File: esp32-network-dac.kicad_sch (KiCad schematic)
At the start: 46 parts, among them J1 USB4510-03-1-A, J2 SJ1-3533NS, J3 Conn_01x04_Male, U1 PCM5122PW, U2 ESP32-WROVER-EM213EH2864PH3Q0, U3 MCP1825S, U4 MCP1825S

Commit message: Changed footrpints to remove DRC warnings. Added board outline.
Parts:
- added H1: MountingHole, symbol Mechanical:MountingHole
- added H2, H3, H4: MountingHole, MountingHole:MountingHole_2.2mm_M2, symbol Mechanical:MountingHole
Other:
- note added: "M2 Mounting Holes"
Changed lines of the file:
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@@
+    (effects (font (size 1.27 1.27) (thickness 0.254) bold) (justify left bottom))
+  )
+  (text "M2 Mounting Holes" (at 133.35 172.72 0)
     (effects (font (size 1.27 1.27) (thickness 0.254) bold) (justify left bottom))
   )
@@
     (pin "1")
   )
+  (symbol (lib_id "Mechanical:MountingHole") (at 135.89 187.96 0) (unit 1)
+    (in_bom yes) (on_board yes) (fields_autoplaced)
+    (property "Reference" "H2" (id 0) (at 138.43 186.6899 0)
+      (effects (font (size 1.27 1.27)) (justify left))
+    )
+    (property "Value" "MountingHole" (id 1) (at 138.43 189.2299 0)
+      (effects (font (size 1.27 1.27)) (justify left))
+    )
+    (property "Footprint" "MountingHole:MountingHole_2.2mm_M2" (id 2) (at 135.89 187.96 0)
+      (effects (font (size 1.27 1.27)) hide)
+    )
+    (property "Datasheet" "~" (id 3) (at 135.89 187.96 0)
+      (effects (font (size 1.27 1.27)) hide)
+    )
+  )
   (symbol (lib_id "power:GND") (at 107.95 134.62 0) (unit 1)
     (in_bom yes) (on_board yes) (fields_autoplaced)
@@
     )
     (pin "1")
+  )
+  (symbol (lib_id "Mechanical:MountingHole") (at 135.89 179.07 0) (unit 1)
+    (in_bom yes) (on_board yes) (fields_autoplaced)
+    (property "Reference" "H1" (id 0) (at 138.43 177.7999 0)
+      (effects (font (size 1.27 1.27)) (justify left))
+    )
+    (property "Value" "MountingHole" (id 1) (at 138.43 180.3399 0)
+      (effects (font (size 1.27 1.27)) (justify left))
+    )
+    (property "Footprint" "" (id 2) (at 135.89 179.07 0)
+      (effects (font (size 1.27 1.27)) hide)
+    )
+    (property "Datasheet" "~" (id 3) (at 135.89 179.07 0)
+      (effects (font (size 1.27 1.27)) hide)
+    )
   )
   (symbol (lib_id "power:+3V3") (at 199.39 20.32 0) (unit 1)
@@
     (pin "2")
   )
+  (symbol (lib_id "Mechanical:MountingHole") (at 154.94 179.07 0) (unit 1)
+    (in_bom yes) (on_board yes) (fields_autoplaced)
+    (property "Reference" "H3" (id 0) (at 157.48 177.7999 0)
+      (effects (font (size 1.27 1.27)) (justify left))
+    )
+    (property "Value" "MountingHole" (id 1) (at 157.48 180.3399 0)
+      (effects (font (size 1.27 1.27)) (justify left))
+    )
+    (property "Footprint" "MountingHole:MountingHole_2.2mm_M2" (id 2) (at 154.94 179.07 0)
+      (effects (font (size 1.27 1.27)) hide)
+    )
+    (property "Datasheet" "~" (id 3) (at 154.94 179.07 0)
+      (effects (font (size 1.27 1.27)) hide)
+    )
+  )
   (symbol (lib_id "power:PWR_FLAG") (at 232.41 144.78 0) (unit 1)
     (in_bom yes) (on_board yes) (fields_autoplaced)
@@
     (pin "3")
     (pin "4")
+  )
+  (symbol (lib_id "Mechanical:MountingHole") (at 154.94 187.96 0) (unit 1)
+    (in_bom yes) (on_board yes) (fields_autoplaced)
+    (property "Reference" "H4" (id 0) (at 157.48 186.6899 0)
+      (effects (font (size 1.27 1.27)) (justify left))
+    )
+    (property "Value" "MountingHole" (id 1) (at 157.48 189.2299 0)
+      (effects (font (size 1.27 1.27)) (justify left))
+    )
+    (property "Footprint" "MountingHole:MountingHole_2.2mm_M2" (id 2) (at 154.94 187.96 0)
+      (effects (font (size 1.27 1.27)) hide)
+    )
+    (property "Datasheet" "~" (id 3) (at 154.94 187.96 0)
+      (effects (font (size 1.27 1.27)) hide)
+    )
   )
   (symbol (lib_id "power:GND") (at 196.85 91.44 0) (unit 1)
@@
       (reference "FB1") (unit 1) (value "120R") (footprint "Resistor_SMD:R_0603_1608Metric")
     )
+    (path "/6d36cd5e-34b5-4051-b036-21bdf59d84b4"
+      (reference "H1") (unit 1) (value "MountingHole") (footprint "MountingHole:MountingHole_2.2mm_M2")
+    )
+    (path "/52e3839b-c2e7-453a-be4e-a57ccb23295f"
+      (reference "H2") (unit 1) (value "MountingHole") (footprint "MountingHole:MountingHole_2.2mm_M2")
+    )
+    (path "/ad63bded-fd94-444e-a2da-8803639d7b67"
+      (reference "H3") (unit 1) (value "MountingHole") (footprint "MountingHole:MountingHole_2.2mm_M2")
+    )
+    (path "/b4c3d837-72a5-4d97-8651-9b49f83ce226"
+      (reference "H4") (unit 1) (value "MountingHole") (footprint "MountingHole:MountingHole_2.2mm_M2")
+    )
     (path "/bccef6fe-1b25-4ae1-a87c-dd8d2ab4d17e"

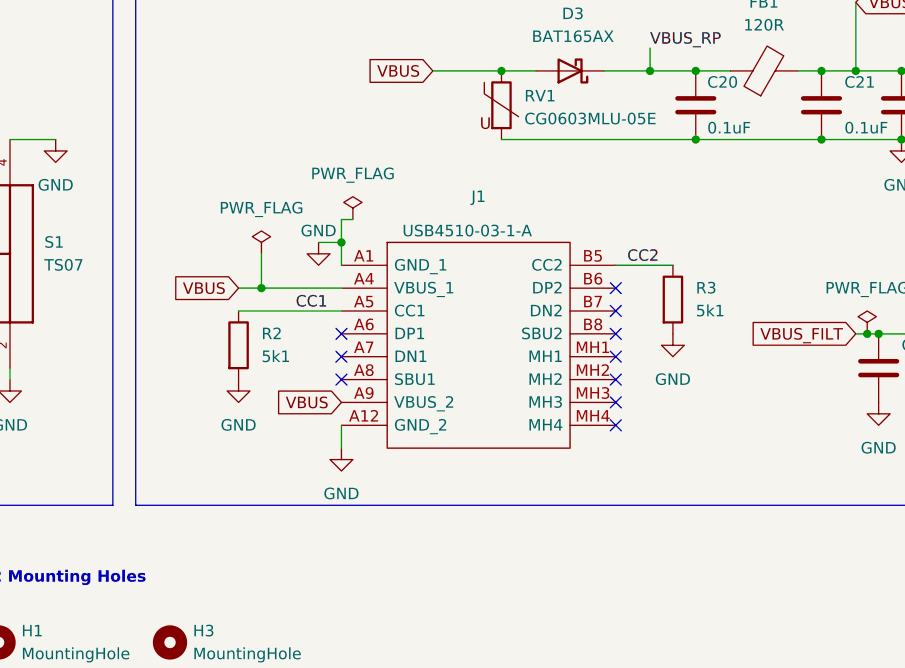
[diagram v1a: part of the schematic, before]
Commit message: Updates to USB C receptive - replaced mid-mount recepticle with SMT
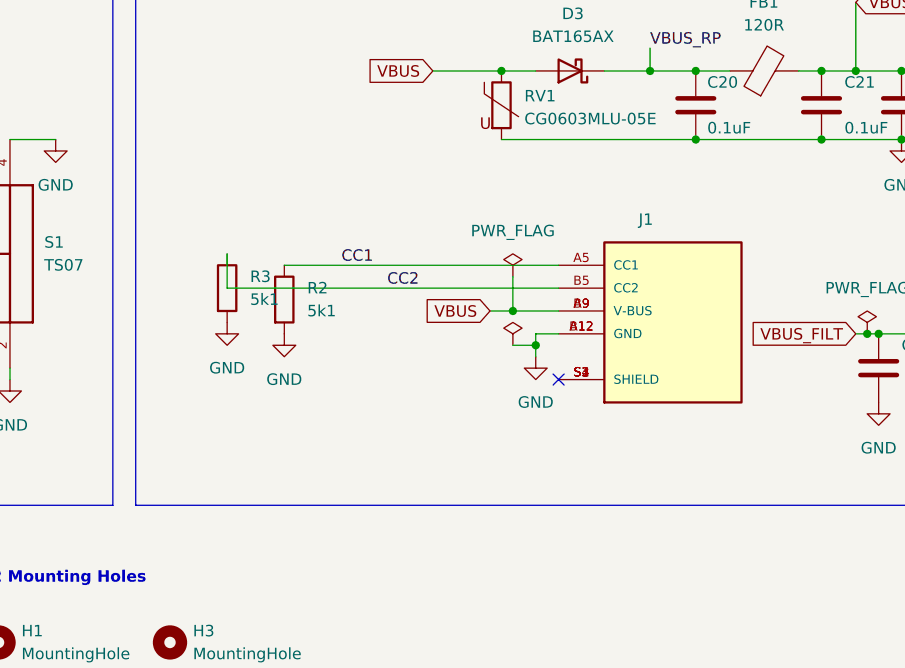
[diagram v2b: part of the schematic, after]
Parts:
- removed J1: USB4510-03-1-A, library:USB4510031A, symbol USB4510-03-1-A:USB4510-03-1-A
- added J1: UJC-HP-3-SMT-TR, library:CUI_UJC-HP-3-SMT-TR, symbol UJC-HP-3-SMT-TR:UJC-HP-3-SMT-TR
- H1: footprint (none) -> MountingHole:MountingHole_2.2mm_M2
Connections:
- net CC1: now also J1.A5 (CC1)
- net CC2: now also J1.B5 (CC2)
- net GND: now also J1.A12 (GND), J1.B12 (GND)
- net VBUS: now also J1.A9 (V-BUS), J1.B9 (V-BUS)
- new net: J1.S1 (SHIELD), J1.S2 (SHIELD), J1.S3 (SHIELD), J1.S4 (SHIELD)
- no-connect marks 28 -> 19

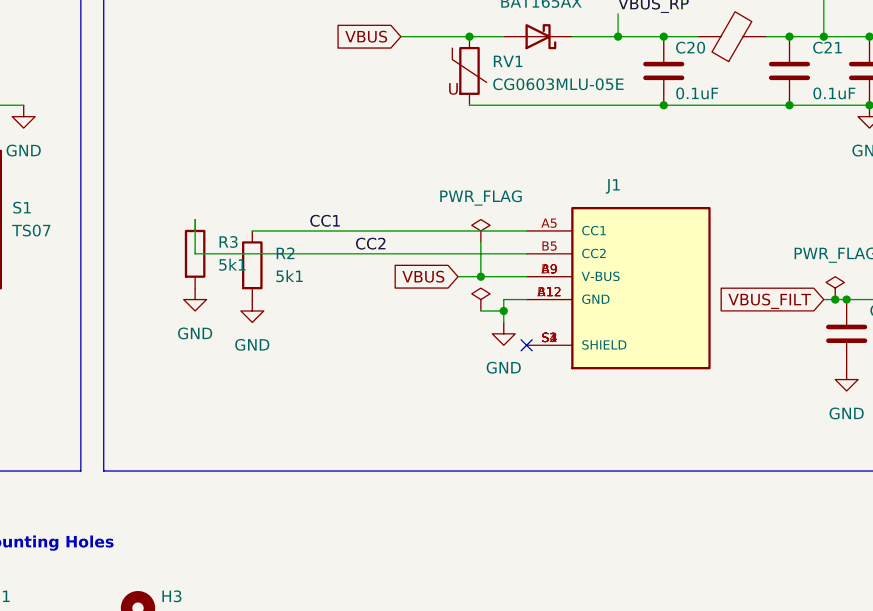
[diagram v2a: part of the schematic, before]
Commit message: Finalised v0.1 design and created manufacturing files
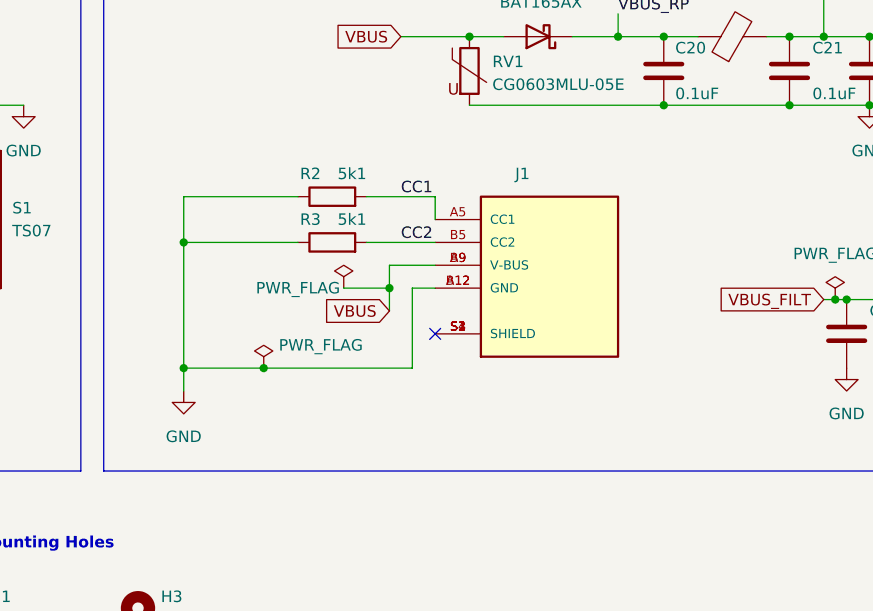
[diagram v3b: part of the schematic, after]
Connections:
- net CC1: now also R2.2; no longer R2.1
- net CC2: now also R3.2; no longer R3.1
- net GND: now also R2.1, R3.1; no longer R2.2, R3.2
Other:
- company: Pavlos Papaefstathiou -> Pavlos P. Lab
- moved on the sheet: J1, R2, R3
